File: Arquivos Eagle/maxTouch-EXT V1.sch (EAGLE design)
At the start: 14 parts

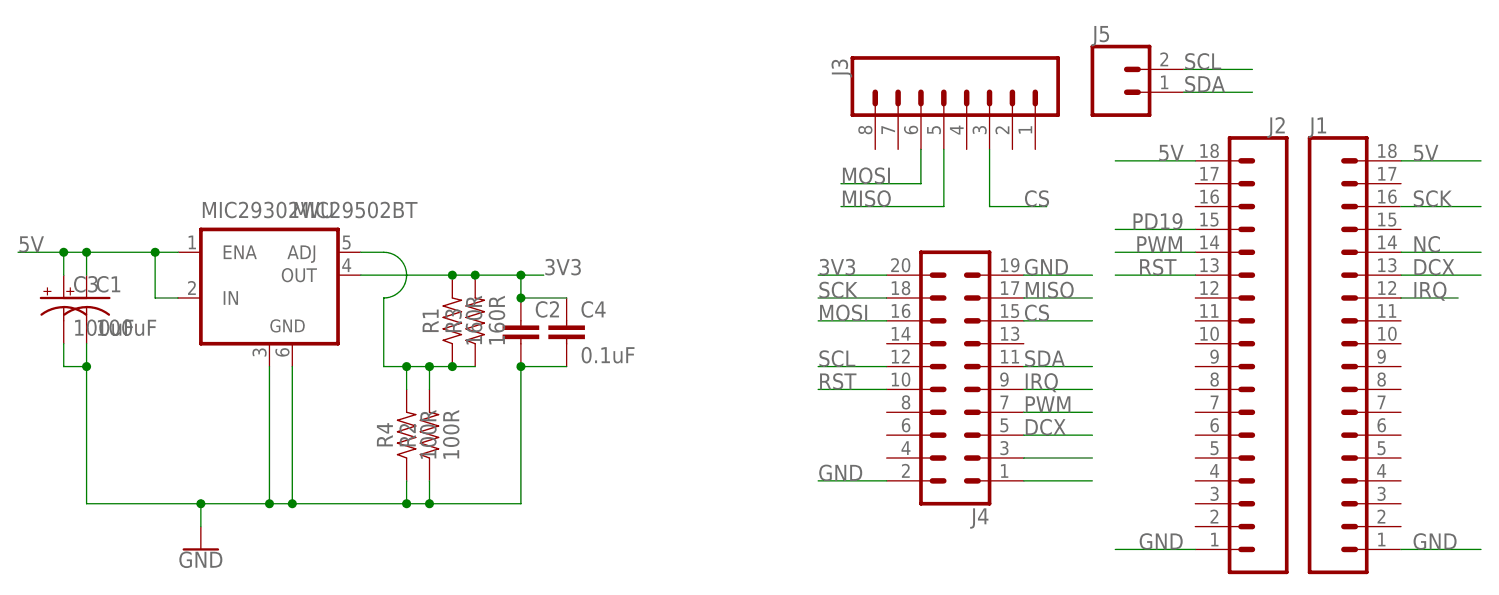
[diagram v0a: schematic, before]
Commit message: Alterado o regulador para obter todos os componentes no Brasil
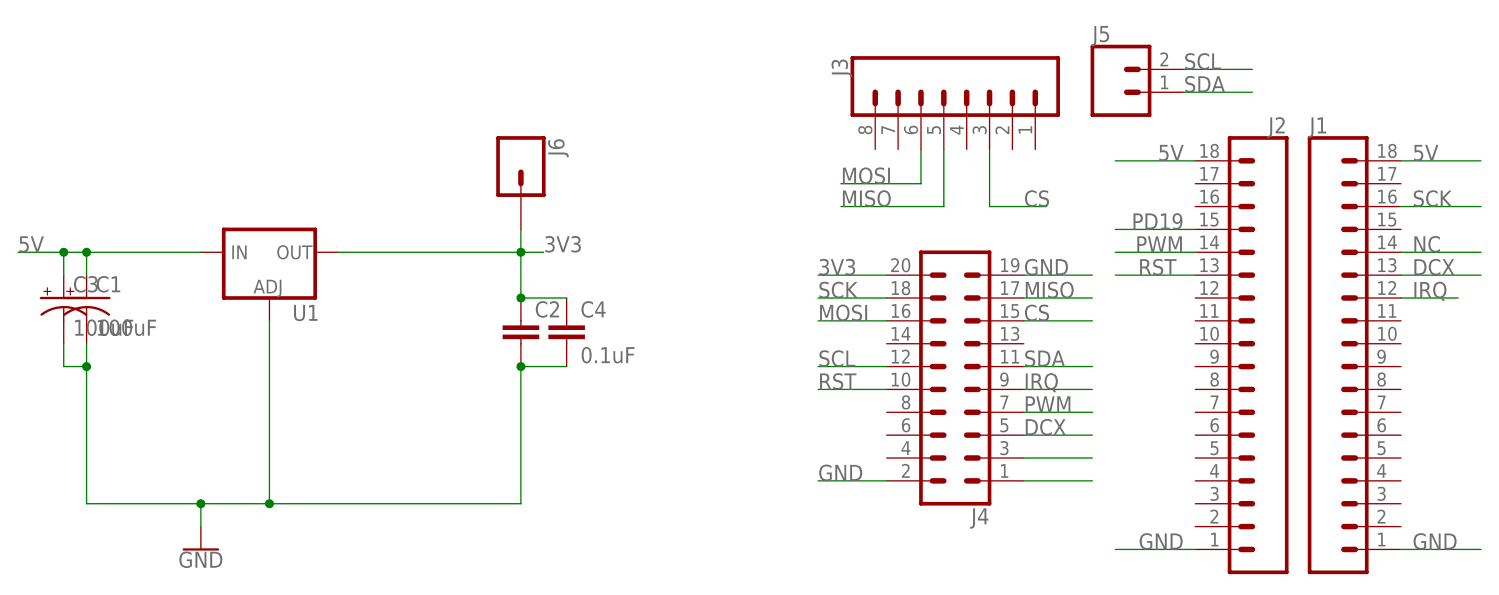
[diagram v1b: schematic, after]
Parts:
- removed MIC29302WU: MIC29502BT, stepper_drivers_etc:MIC29502BT
- removed R1: 160R, SparkFun-Resistors:RESISTOR1206
- removed R2: 100R, SparkFun-Resistors:RESISTOR1206
- removed R3: 160R, SparkFun-Resistors:RESISTORAXIAL-0.3-KIT
- removed R4: 100R, SparkFun-Resistors:RESISTORAXIAL-0.3-KIT
- added J6: (no value), SparkFun-Connectors:CONN_01
- added U1: (no value), SparkFun-IC-Power:V_REG_LM1117SOT223
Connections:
- removed net N$2: MIC29302WU.ADJ, R1.1, R2.2, R3.1, R4.2
- net 3V3: now also J6.1, U1.OUT; no longer MIC29302WU.OUT, R1.2, R3.2
- net 5V: now also U1.IN; no longer MIC29302WU.ENA, MIC29302WU.IN
- net GND: now also U1.ADJ; no longer MIC29302WU.GND, MIC29302WU.GND@1, R2.1, R4.1

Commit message: ~
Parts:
- C2: device SparkFun-Capacitors:CAP-1206 -> SparkFun-Capacitors:CAP-0805
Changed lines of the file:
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@@
 <part name="J5" library="SparkFun-Connectors" library_urn="urn:adsk.eagle:library:3489003" deviceset="CONN_02" device="" package3d_urn="urn:adsk.eagle:package:3489464/1"/>
 <part name="C1" library="SparkFun-Capacitors" deviceset="100UF-POLAR" device="-25V-20%(ELEC)" value="100uF"/>
-<part name="C2" library="SparkFun-Capacitors" deviceset="CAP" device="-1206" value="10uF"/>
+<part name="C2" library="SparkFun-Capacitors" deviceset="CAP" device="-0805" value="10uF"/>
 <part name="GND1" library="SparkFun-PowerSymbols" deviceset="GND" device=""/>
 <part name="C3" library="SparkFun-Capacitors" deviceset="100UF-POLAR" device="-RADIAL-2.5MM-25V-20%" value="100uF"/>

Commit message: Pequenas Alterações no .brd
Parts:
- C1: device SparkFun-Capacitors:100UF-POLAR-25V-20%(ELEC) -> SparkFun-Capacitors:100UF-POLAR-10X10.5-63V-20%
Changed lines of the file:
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@@
 <part name="J4" library="SparkFun-Connectors" library_urn="urn:adsk.eagle:library:3489003" deviceset="CONN_10X2" device="" package3d_urn="urn:adsk.eagle:package:3489558/1"/>
 <part name="J5" library="SparkFun-Connectors" library_urn="urn:adsk.eagle:library:3489003" deviceset="CONN_02" device="" package3d_urn="urn:adsk.eagle:package:3489464/1"/>
-<part name="C1" library="SparkFun-Capacitors" deviceset="100UF-POLAR" device="-25V-20%(ELEC)" value="100uF"/>
+<part name="C1" library="SparkFun-Capacitors" deviceset="100UF-POLAR" device="-10X10.5-63V-20%" value="100uF"/>
 <part name="C2" library="SparkFun-Capacitors" deviceset="CAP" device="-0805" value="10uF"/>
 <part name="GND1" library="SparkFun-PowerSymbols" deviceset="GND" device=""/>

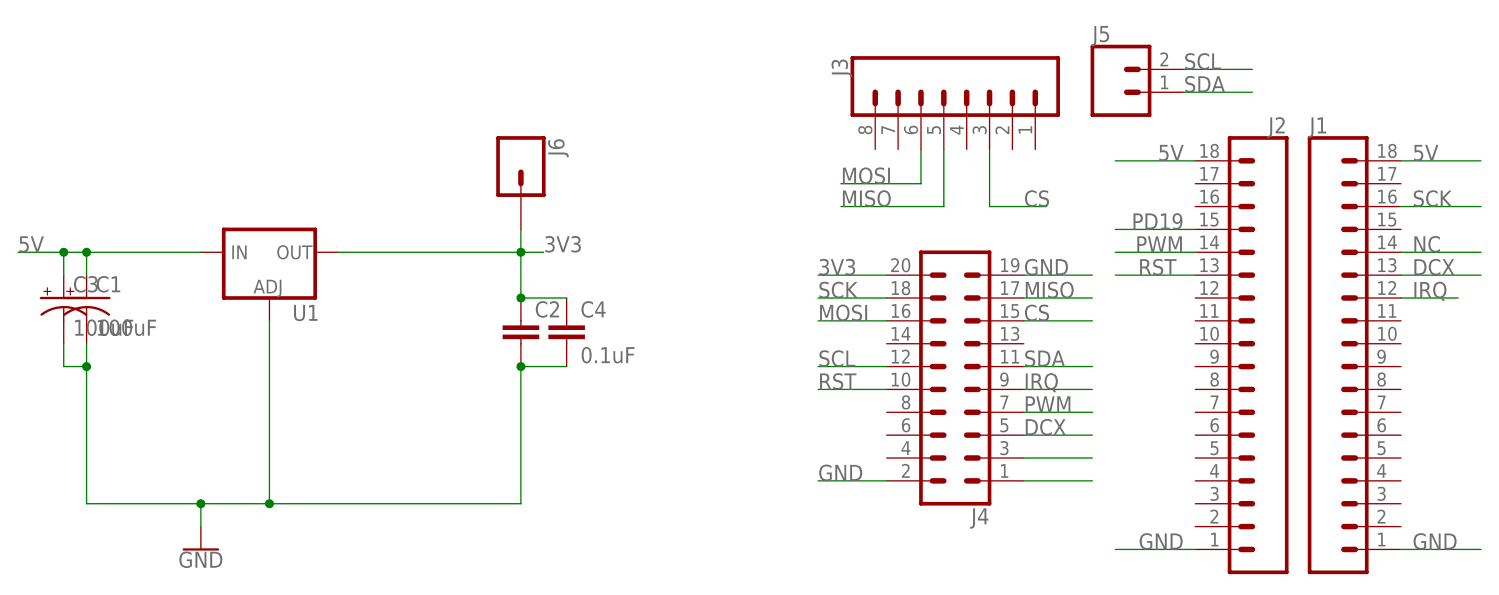
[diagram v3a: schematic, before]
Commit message: Pequenas alteracoes no Layout
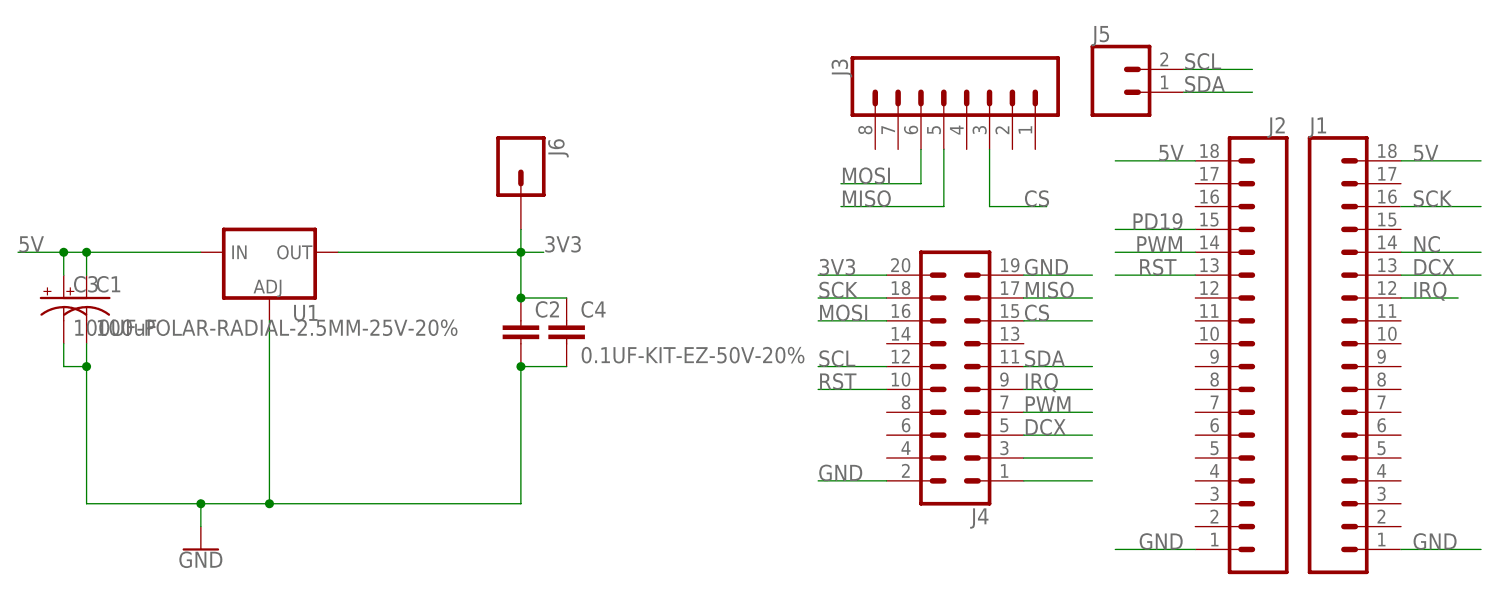
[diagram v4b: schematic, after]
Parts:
- C3: value 100uF -> 100UF-POLAR-RADIAL-2.5MM-25V-20%
- C4: value 0.1uF -> 0.1UF-KIT-EZ-50V-20%
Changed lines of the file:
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@@
 <part name="C2" library="SparkFun-Capacitors" deviceset="CAP" device="-0805" value="10uF"/>
 <part name="GND1" library="SparkFun-PowerSymbols" deviceset="GND" device=""/>
-<part name="C3" library="SparkFun-Capacitors" deviceset="100UF-POLAR" device="-RADIAL-2.5MM-25V-20%" value="100uF"/>
-<part name="C4" library="SparkFun-Capacitors" deviceset="0.1UF" device="-KIT-EZ-50V-20%" value="0.1uF"/>
+<part name="C3" library="SparkFun-Capacitors" deviceset="100UF-POLAR" device="-RADIAL-2.5MM-25V-20%" value="100UF-POLAR-RADIAL-2.5MM-25V-20%"/>
+<part name="C4" library="SparkFun-Capacitors" deviceset="0.1UF" device="-KIT-EZ-50V-20%" value="0.1UF-KIT-EZ-50V-20%"/>
 <part name="U1" library="SparkFun-IC-Power" deviceset="V_REG_LM1117" device="SOT223"/>
 <part name="J6" library="SparkFun-Connectors" deviceset="CONN_01" device=""/>
